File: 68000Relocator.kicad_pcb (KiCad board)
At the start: 2 copper layers, 97.4 x 94.7 mm, 3 parts, among them P99 OSHW_LOGO, U1 68000D, U2 68000D

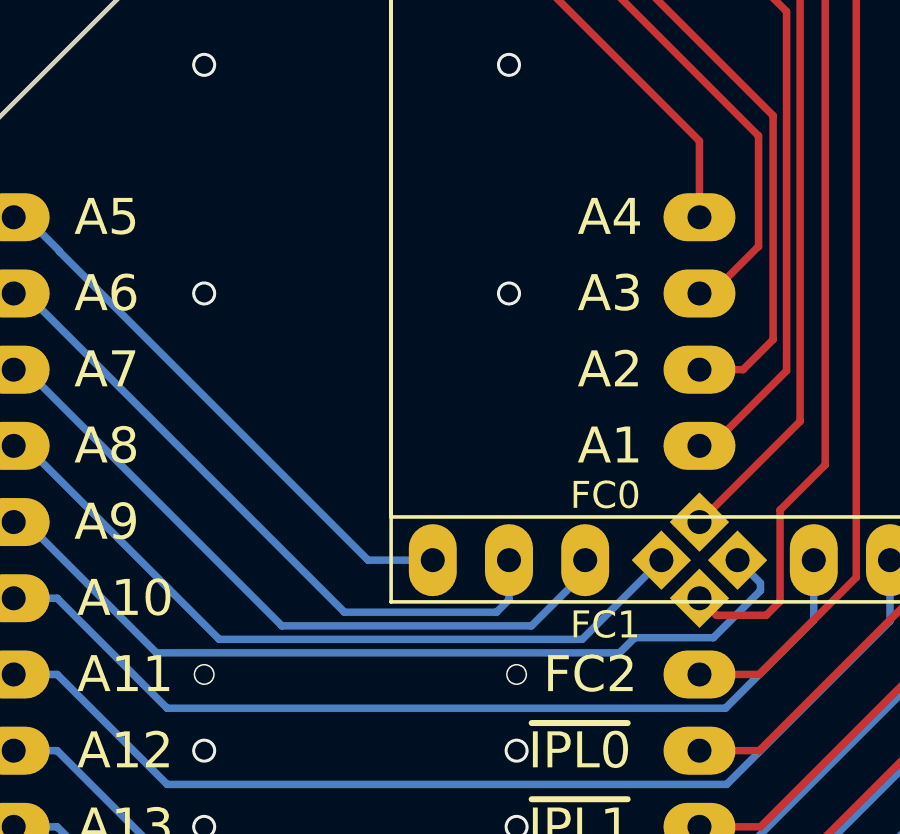
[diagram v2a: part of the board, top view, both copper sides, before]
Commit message: Create test points for pins covered by CPU
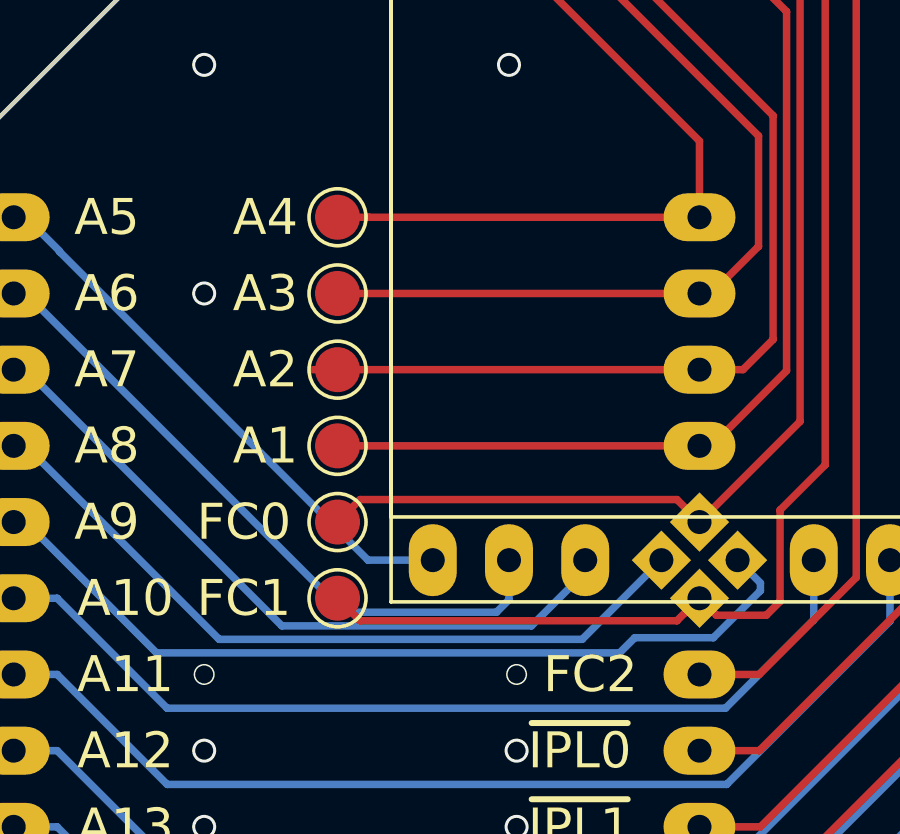
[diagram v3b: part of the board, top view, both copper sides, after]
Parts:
- added TP1: TestPoint, TestPoint:TestPoint_Pad_D1.5mm, F.Cu at (103.0, 73.9)
- added TP2: TestPoint, TestPoint:TestPoint_Pad_D1.5mm, F.Cu at (103.0, 71.4)
- added TP3: TestPoint, TestPoint:TestPoint_Pad_D1.5mm, F.Cu at (103.0, 68.8)
- added TP4: TestPoint, TestPoint:TestPoint_Pad_D1.5mm, F.Cu at (103.0, 66.3)
- added TP5: TestPoint, TestPoint:TestPoint_Pad_D1.5mm, F.Cu at (103.0, 63.8)
- added TP6: TestPoint, TestPoint:TestPoint_Pad_D1.5mm, F.Cu at (103.0, 61.2)
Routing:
- net /A2: track 21.0 -> 34.1 mm
- net /FC1: track 28.1 -> 40.8 mm
- net /FC0: track 23.8 -> 36.5 mm
- net /A1: track 22.2 -> 34.3 mm
- net /A4: track 15.3 -> 27.4 mm
- net /A3: track 18.5 -> 30.5 mm
- net GND: vias 72 -> 71
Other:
- board text added: "V2"
- board text removed: "V1"
